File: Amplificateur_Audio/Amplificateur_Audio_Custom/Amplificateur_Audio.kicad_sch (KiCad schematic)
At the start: 0 parts

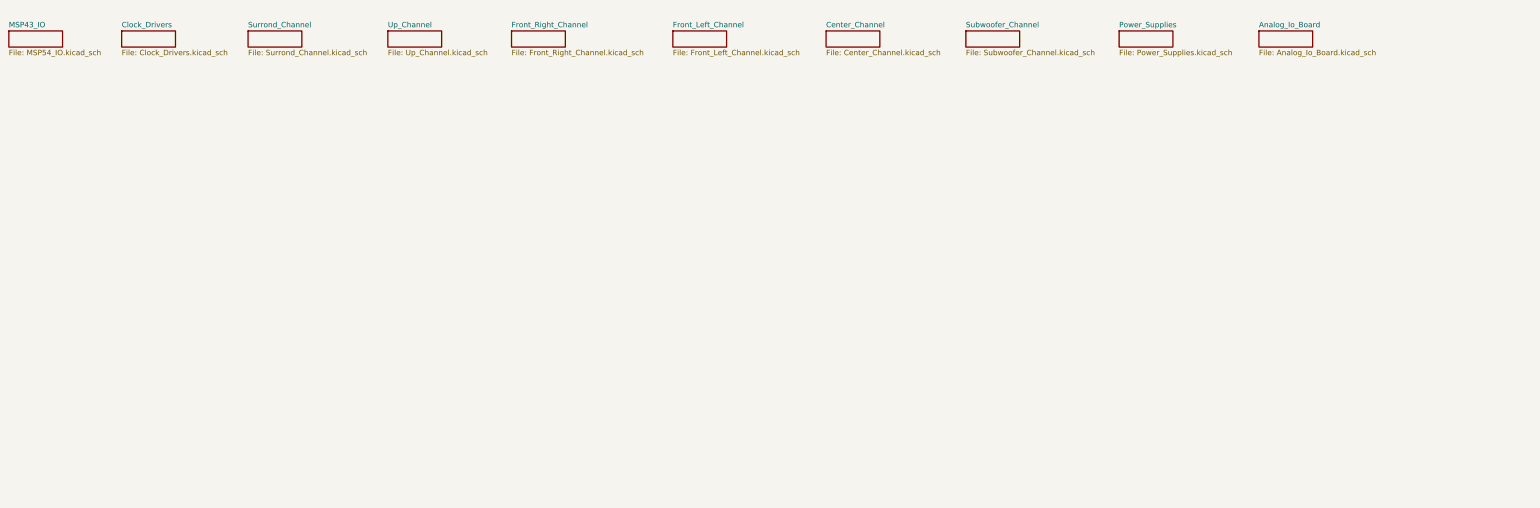
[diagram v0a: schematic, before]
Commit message: Refactor : hierarchical template channels for multichannel routing
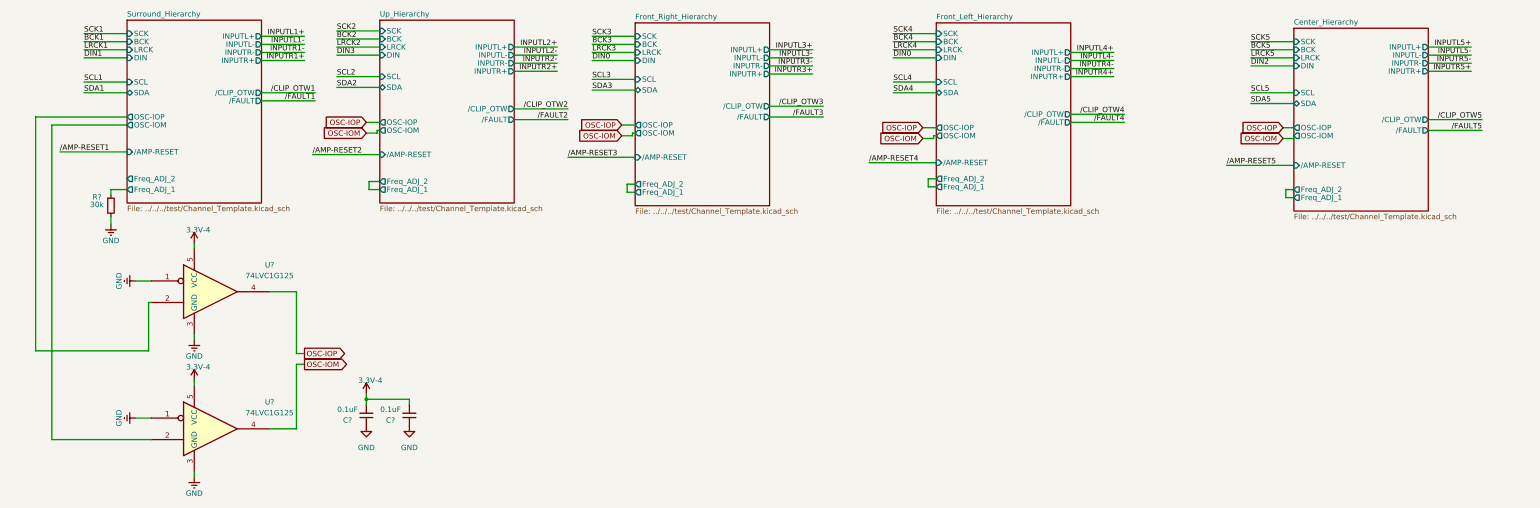
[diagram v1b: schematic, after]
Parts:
- added C? (x2): 0.1uF, Capacitor_SMD:C_0402_1005Metric, symbol Device:C_Small
- added R?: 30k, Resistor_SMD:R_0603_1608Metric, symbol Device:R_Small
- added U? (x2): 74LVC1G125, Package_TO_SOT_SMD:SOT-353_SC-70-5_Handsoldering, symbol 74xGxx:LVC1G125Ti
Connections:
- new net 3.3V-4: C?.2, C?.2, U?.5 (VCC), U?.5 (VCC)
- new net GND: C?.1, C?.1, R?.2, U?.1, U?.1, U?.3 (GND), U?.3 (GND)
- new net OSC-IOM: U?.4
- new net OSC-IOP: U?.4
- new net Surround_Hierarchy/Freq_ADJ_1: R?.1
- new net Surround_Hierarchy/OSC-IOM: U?.2
- new net Surround_Hierarchy/OSC-IOP: U?.2
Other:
- removed sheet Analog_Io_Board
- removed sheet Center_Channel
- removed sheet Clock_Drivers
- removed sheet Front_Left_Channel
- removed sheet Front_Right_Channel
- removed sheet MSP43_IO
- removed sheet Power_Supplies
- removed sheet Subwoofer_Channel
- removed sheet Surrond_Channel
- removed sheet Up_Channel
- added sheet Center_Hierarchy (../../../test/Channel_Template.kicad_sch)
- added sheet Front_Left_Hierarchy (../../../test/Channel_Template.kicad_sch)
- added sheet Front_Right_Hierarchy (../../../test/Channel_Template.kicad_sch)
- added sheet Surround_Hierarchy (../../../test/Channel_Template.kicad_sch)
- added sheet Up_Hierarchy (../../../test/Channel_Template.kicad_sch)

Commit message: Factorisation réussite et validation de la duplication de channel
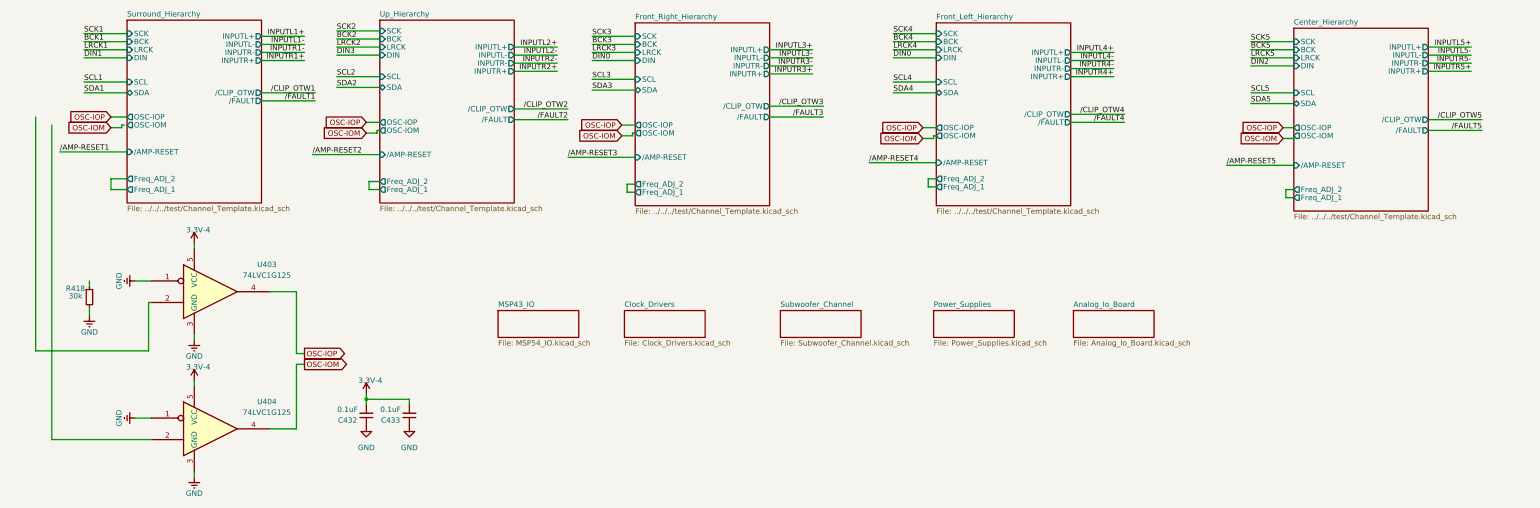
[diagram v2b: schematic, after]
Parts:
- gave numbers to parts that had none: 5
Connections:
- net Surround_Hierarchy/Freq_ADJ_1: no longer R418.1
- net Surround_Hierarchy/OSC-IOM: no longer U404.2
- net Surround_Hierarchy/OSC-IOP: no longer names the net of U403.2
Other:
- added sheet Analog_Io_Board (Analog_Io_Board.kicad_sch)
- added sheet Clock_Drivers (Clock_Drivers.kicad_sch)
- added sheet MSP43_IO (MSP54_IO.kicad_sch)
- added sheet Power_Supplies (Power_Supplies.kicad_sch)
- added sheet Subwoofer_Channel (Subwoofer_Channel.kicad_sch)
- moved on the sheet: R418
